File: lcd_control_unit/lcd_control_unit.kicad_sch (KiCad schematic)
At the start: 9 parts, among them J1 Conn_01x05_Socket, J2 Conn_01x02_Socket, J3 Conn_01x02_Socket, J4 Conn_01x02_Socket, J5 Conn_01x02_Socket, J6 Conn_01x03_Socket, J7 Conn_01x010_Socket, Q1 2N2222

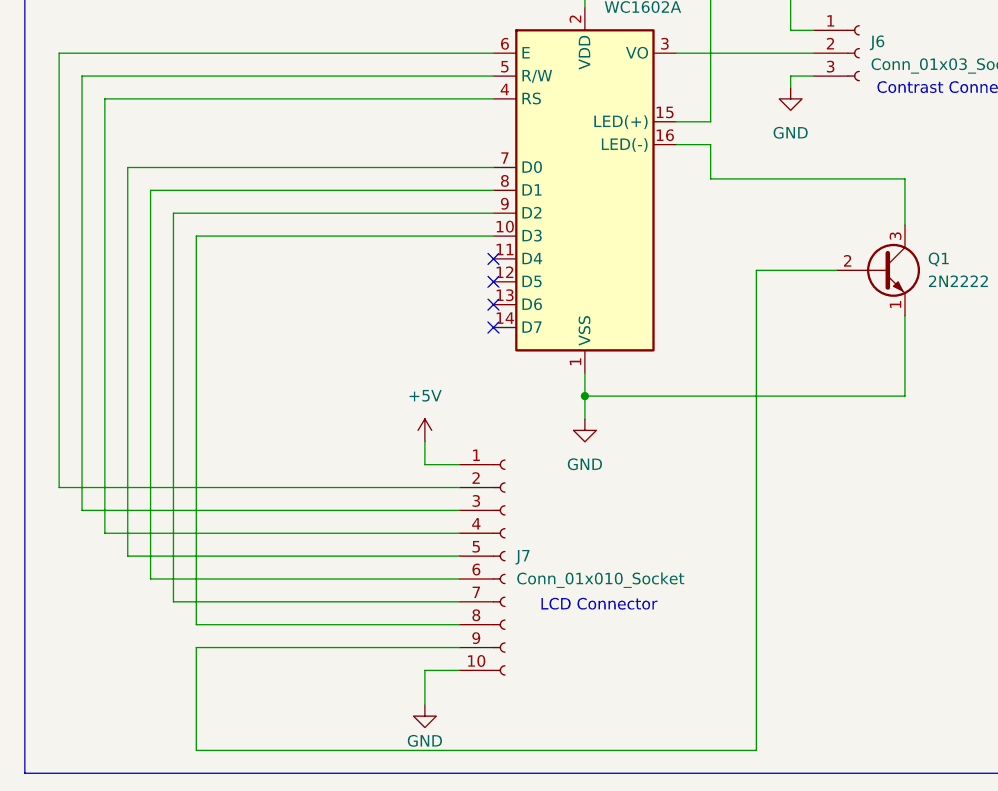
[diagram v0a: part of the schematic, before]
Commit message: fix: back light circuitry and data lines
A resistor was missing for the base of the transistor. The data lines
were also not wired correctly

Signed-off-by: Scott Gibb <smgibb@yahoo.com>
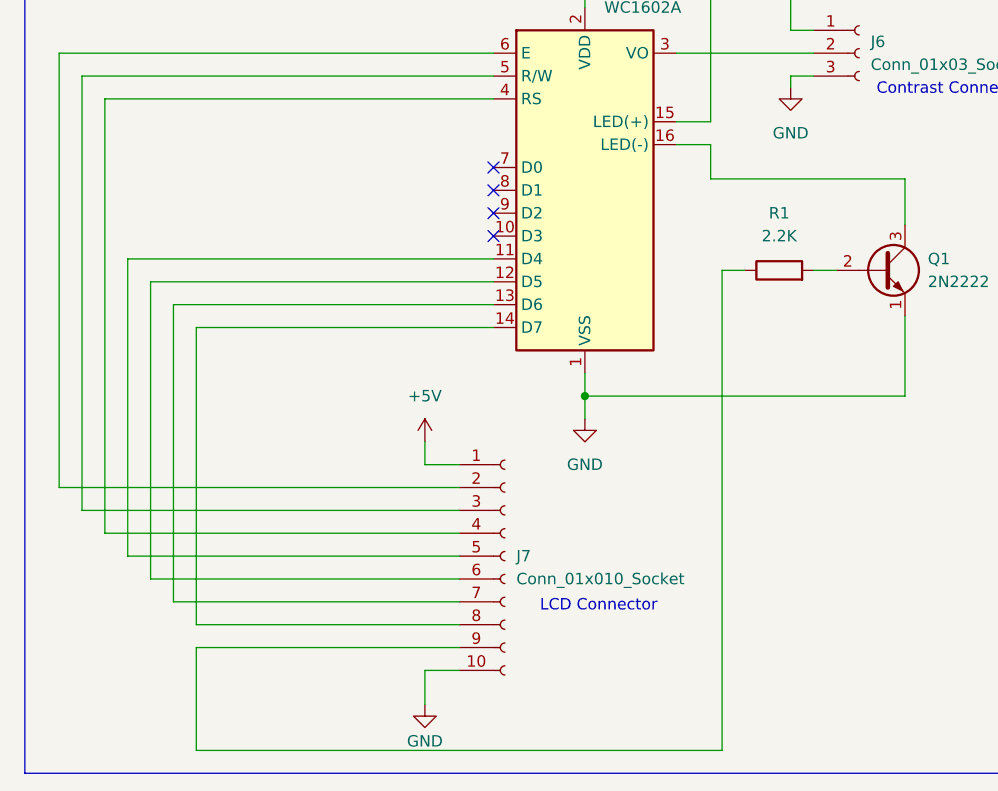
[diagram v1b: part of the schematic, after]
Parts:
- added R1: 2.2K, symbol Device:R
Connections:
- net at J7.9 (Pin_9): now also R1.1; no longer Q1.2 (B)
- net at DS1.10 (D3): no longer J7.8 (Pin_8)
- net at DS1.11 (D4): now also J7.5 (Pin_5)
- net at DS1.12 (D5): now also J7.6 (Pin_6)
- net at DS1.13 (D6): now also J7.7 (Pin_7)
- net at DS1.14 (D7): now also J7.8 (Pin_8)
- net at DS1.7 (D0): no longer J7.5 (Pin_5)
- net at DS1.8 (D1): no longer J7.6 (Pin_6)
- net at DS1.9 (D2): no longer J7.7 (Pin_7)
- new net: Q1.2 (B), R1.2
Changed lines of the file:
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@@
 	)
 	(no_connect
-		(at 66.04 63.5)
+		(at 66.04 50.8)
 	)
 	(no_connect
-		(at 66.04 58.42)
+		(at 66.04 48.26)
 	)
 	(no_connect
-		(at 66.04 66.04)
+		(at 66.04 55.88)
 	)
 	(no_connect
-		(at 66.04 60.96)
+		(at 66.04 53.34)
 	)
 	(wire
@@
 	(wire
 		(pts
-			(xy 66.04 53.34) (xy 30.48 53.34)
-		)
-		(stroke
-			(width 0)
-			(type default)
-		)
-	)
-	(wire
-		(pts
 			(xy 231.14 80.01) (xy 231.14 76.2)
 		)
@@
 	(wire
 		(pts
+			(xy 91.44 59.69) (xy 93.98 59.69)
+		)
+		(stroke
+			(width 0)
+			(type default)
+		)
+	)
+	(wire
+		(pts
 			(xy 90.17 49.53) (xy 111.76 49.53)
 		)
@@
 	(wire
 		(pts
+			(xy 101.6 59.69) (xy 104.14 59.69)
+		)
+		(stroke
+			(width 0)
+			(type default)
+		)
+	)
+	(wire
+		(pts
 			(xy 33.02 113.03) (xy 33.02 101.6)
 		)
@@
 	(wire
 		(pts
-			(xy 27.94 50.8) (xy 27.94 93.98)
-		)
-		(stroke
-			(width 0)
-			(type default)
-		)
-	)
-	(wire
-		(pts
-			(xy 33.02 55.88) (xy 33.02 99.06)
-		)
-		(stroke
-			(width 0)
-			(type default)
-		)
-	)
-	(wire
-		(pts
 			(xy 138.43 73.66) (xy 233.68 73.66)
 		)
@@
 	(wire
 		(pts
-			(xy 66.04 50.8) (xy 27.94 50.8)
-		)
-		(stroke
-			(width 0)
-			(type default)
-		)
-	)
-	(wire
-		(pts
-			(xy 25.4 48.26) (xy 25.4 91.44)
-		)
-		(stroke
-			(width 0)
-			(type default)
-		)
-	)
-	(wire
-		(pts
 			(xy 228.6 49.53) (xy 224.79 49.53)
 		)
@@
 	(wire
 		(pts
-			(xy 66.04 48.26) (xy 25.4 48.26)
+			(xy 66.04 66.04) (xy 33.02 66.04)
 		)
 		(stroke
@@
 	(wire
 		(pts
-			(xy 30.48 53.34) (xy 30.48 96.52)
-		)
-		(stroke
-			(width 0)
-			(type default)
-		)
-	)
-	(wire
-		(pts
-			(xy 66.04 55.88) (xy 33.02 55.88)
-		)
-		(stroke
-			(width 0)
-			(type default)
-		)
-	)
-	(wire
-		(pts
 			(xy 33.02 101.6) (xy 62.23 101.6)
 		)
@@
 	(wire
 		(pts
-			(xy 95.25 113.03) (xy 33.02 113.03)
+			(xy 91.44 113.03) (xy 33.02 113.03)
 		)
 		(stroke
@@
 	(wire
 		(pts
+			(xy 27.94 60.96) (xy 27.94 93.98)
+		)
+		(stroke
+			(width 0)
+			(type default)
+		)
+	)
+	(wire
+		(pts
 			(xy 86.36 43.18) (xy 90.17 43.18)
 		)
@@
 	(wire
 		(pts
+			(xy 25.4 58.42) (xy 66.04 58.42)
+		)
+		(stroke
+			(width 0)
+			(type default)
+		)
+	)
+	(wire
+		(pts
 			(xy 111.76 64.77) (xy 111.76 73.66)
 		)
@@
 	(wire
 		(pts
+			(xy 30.48 63.5) (xy 30.48 96.52)
+		)
+		(stroke
+			(width 0)
+			(type default)
+		)
+	)
+	(wire
+		(pts
 			(xy 224.79 27.94) (xy 227.33 27.94)
 		)
@@
 	(wire
 		(pts
-			(xy 104.14 59.69) (xy 95.25 59.69)
-		)
-		(stroke
-			(width 0)
-			(type default)
-		)
-	)
-	(wire
-		(pts
 			(xy 17.78 83.82) (xy 62.23 83.82)
 		)
@@
 	(wire
 		(pts
+			(xy 33.02 66.04) (xy 33.02 99.06)
+		)
+		(stroke
+			(width 0)
+			(type default)
+		)
+	)
+	(wire
+		(pts
 			(xy 17.78 35.56) (xy 17.78 83.82)
 		)
@@
 	(wire
 		(pts
+			(xy 27.94 60.96) (xy 66.04 60.96)
+		)
+		(stroke
+			(width 0)
+			(type default)
+		)
+	)
+	(wire
+		(pts
 			(xy 90.17 24.13) (xy 90.17 25.4)
 		)
@@
 	(wire
 		(pts
-			(xy 95.25 59.69) (xy 95.25 113.03)
+			(xy 91.44 59.69) (xy 91.44 113.03)
 		)
 		(stroke
@@
 	(wire
 		(pts
+			(xy 25.4 58.42) (xy 25.4 91.44)
+		)
+		(stroke
+			(width 0)
+			(type default)
+		)
+	)
+	(wire
+		(pts
 			(xy 170.18 50.8) (xy 167.64 50.8)
 		)
@@
 		(pts
 			(xy 228.6 46.99) (xy 200.66 46.99)
+		)
+		(stroke
+			(width 0)
+			(type default)
+		)
+	)
+	(wire
+		(pts
+			(xy 66.04 63.5) (xy 30.48 63.5)
 		)
 		(stroke
@@
 		)
 		(instances
-			(project "home_power_monitor_hardware"
+			(project "lcd_control_unit"
 				(path "/6b50284b-05e1-4845-9c49-b3a0e910d486"
 					(reference "#PWR05")
@@
 		)
 		(instances
-			(project "home_power_monitor_hardware"
+			(project "lcd_control_unit"
 				(path "/6b50284b-05e1-4845-9c49-b3a0e910d486"
 					(reference "J1")
@@
 		)
 		(instances
-			(project "home_power_monitor_hardware"
+			(project "lcd_control_unit"
 				(path "/6b50284b-05e1-4845-9c49-b3a0e910d486"
 					(reference "#PWR06")
+					(unit 1)
+				)
+			)
+		)
+	)
+	(symbol
+		(lib_id "Device:R")
+		(at 97.79 59.69 90)
+		(unit 1)
+		(body_style 1)
+		(exclude_from_sim no)
+		(in_bom yes)
+		(on_board yes)
+		(in_pos_files yes)
+		(dnp no)
+		(fields_autoplaced yes)
+		(property "Reference" "R1"
+			(at 97.79 53.34 90)
+			(show_name no)
+			(do_not_autoplace no)
+			(effects
+				(font
+					(size 1.27 1.27)
+				)
+			)
+		)
+		(property "Value" "2.2K"
+			(at 97.79 55.88 90)
+			(show_name no)
+			(do_not_autoplace no)
+			(effects
+				(font
+					(size 1.27 1.27)
+				)
+			)
+		)
+		(property "Footprint" ""
+			(at 97.79 61.468 90)
+			(hide yes)
+			(show_name no)
+			(do_not_autoplace no)
+			(effects
+				(font
+					(size 1.27 1.27)
+				)
+			)
+		)
+		(property "Datasheet" ""
+			(at 97.79 59.69 0)
+			(hide yes)
+			(show_name no)
+			(do_not_autoplace no)
+			(effects
+				(font
+					(size 1.27 1.27)
+				)
+			)
+		)
+		(property "Description" "Resistor"
+			(at 97.79 59.69 0)
+			(hide yes)
+			(show_name no)
+			(do_not_autoplace no)
+			(effects
+				(font
+					(size 1.27 1.27)
+				)
+			)
+		)
+		(pin "1"
+		)
+		(pin "2"
+		)
+		(instances
+			(project "lcd_control_unit"
+				(path "/6b50284b-05e1-4845-9c49-b3a0e910d486"
+					(reference "R1")
 					(unit 1)
 				)
@@
 		)
 		(instances
-			(project "home_power_monitor_hardware"
+			(project "lcd_control_unit"
 				(path "/6b50284b-05e1-4845-9c49-b3a0e910d486"
 					(reference "Q1")
@@
 		)
 		(instances
-			(project "home_power_monitor_hardware"
+			(project "lcd_control_unit"
 				(path "/6b50284b-05e1-4845-9c49-b3a0e910d486"
 					(reference "J6")
@@
 		)
 		(instances
-			(project "home_power_monitor_hardware"
+			(project "lcd_control_unit"
 				(path "/6b50284b-05e1-4845-9c49-b3a0e910d486"
 					(reference "#PWR08")
@@
 		)
 		(instances
-			(project "home_power_monitor_hardware"
+			(project "lcd_control_unit"
 				(path "/6b50284b-05e1-4845-9c49-b3a0e910d486"
 					(reference "DS1")
@@
 		)
 		(instances
-			(project "home_power_monitor_hardware"
+			(project "lcd_control_unit"
 				(path "/6b50284b-05e1-4845-9c49-b3a0e910d486"
 					(reference "J2")
@@
 		)
 		(instances
-			(project "home_power_monitor_hardware"
+			(project "lcd_control_unit"
 				(path "/6b50284b-05e1-4845-9c49-b3a0e910d486"
 					(reference "J3")
@@
 		)
 		(instances
-			(project "home_power_monitor_hardware"
+			(project "lcd_control_unit"
 				(path "/6b50284b-05e1-4845-9c49-b3a0e910d486"
 					(reference "J5")
@@
 		)
 		(instances
-			(project "home_power_monitor_hardware"
+			(project "lcd_control_unit"
 				(path "/6b50284b-05e1-4845-9c49-b3a0e910d486"
 					(reference "#PWR02")
@@
 		)
 		(instances
-			(project "home_power_monitor_hardware"
+			(project "lcd_control_unit"
 				(path "/6b50284b-05e1-4845-9c49-b3a0e910d486"
 					(reference "#PWR04")
@@
 		)
 		(instances
-			(project "home_power_monitor_hardware"
+			(project "lcd_control_unit"
 				(path "/6b50284b-05e1-4845-9c49-b3a0e910d486"
 					(reference "#PWR03")
@@
 		)
 		(instances
-			(project "home_power_monitor_hardware"
+			(project "lcd_control_unit"
 				(path "/6b50284b-05e1-4845-9c49-b3a0e910d486"
 					(reference "J7")
@@
 		)
 		(instances
-			(project "home_power_monitor_hardware"
+			(project "lcd_control_unit"
 				(path "/6b50284b-05e1-4845-9c49-b3a0e910d486"
 					(reference "#PWR07")
@@
 		)
 		(instances
-			(project "home_power_monitor_hardware"
+			(project "lcd_control_unit"
 				(path "/6b50284b-05e1-4845-9c49-b3a0e910d486"
 					(reference "#PWR09")
@@
 		)
 		(instances
-			(project "home_power_monitor_hardware"
+			(project "lcd_control_unit"
 				(path "/6b50284b-05e1-4845-9c49-b3a0e910d486"
 					(reference "J4")

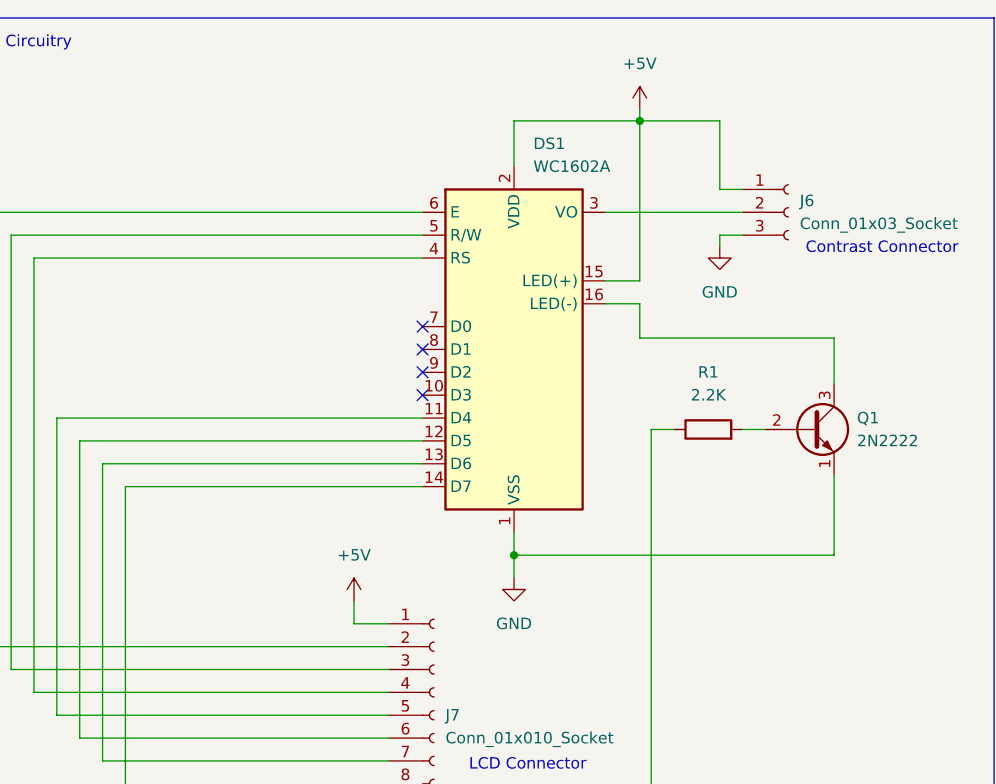
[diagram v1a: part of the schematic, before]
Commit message: feat: add decoupling caps to lcd control unit circuitry
Signed-off-by: Scott Gibb <smgibb@yahoo.com>
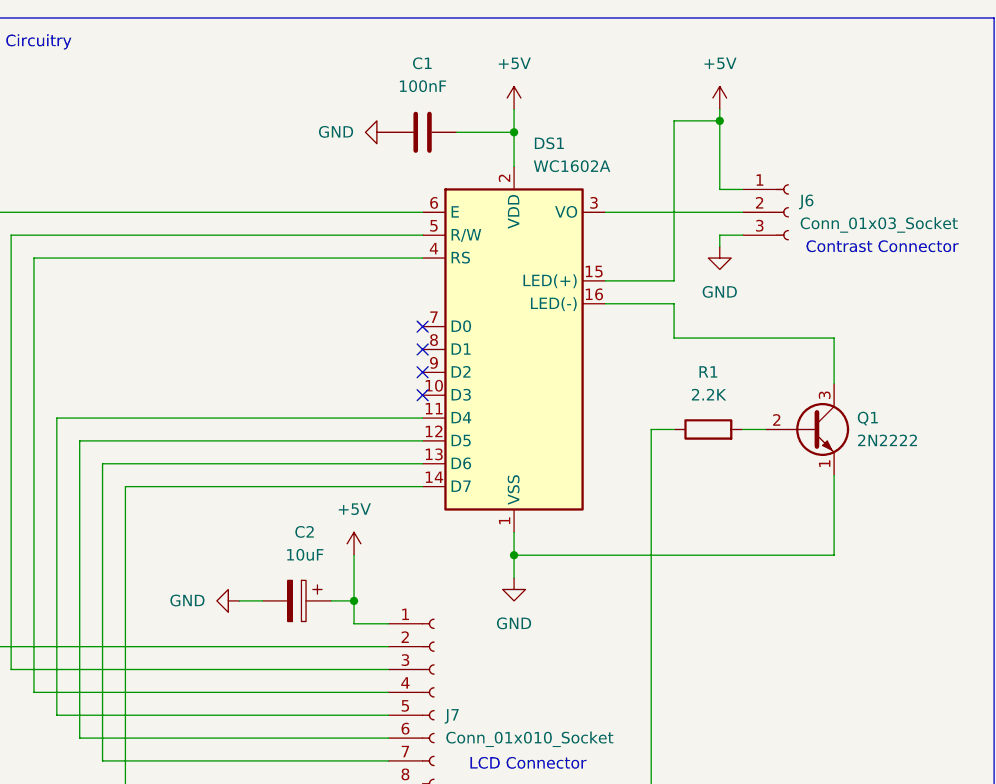
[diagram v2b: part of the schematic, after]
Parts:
- added C1: 100nF, symbol Device:C
- added C2: 10uF, symbol Device:C_Polarized
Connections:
- net +5V: now also C1.1, C2.1
- net GND: now also C1.2, C2.2
